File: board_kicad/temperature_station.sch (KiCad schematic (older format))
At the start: 3 parts, among them U1 WeMos_D1_mini, U2 DHT11

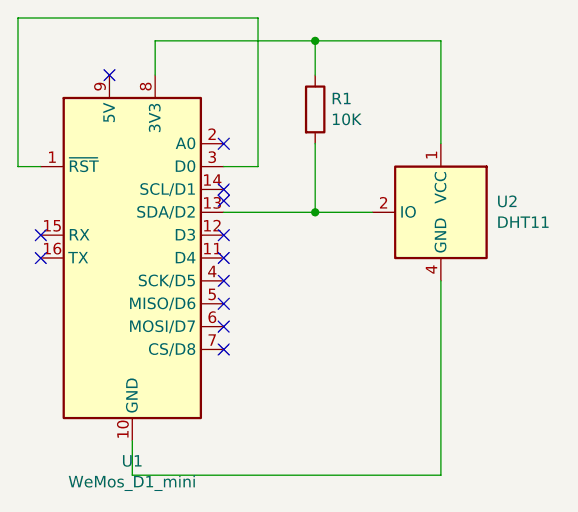
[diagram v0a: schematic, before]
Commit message: Changed DHT11 to DHT22
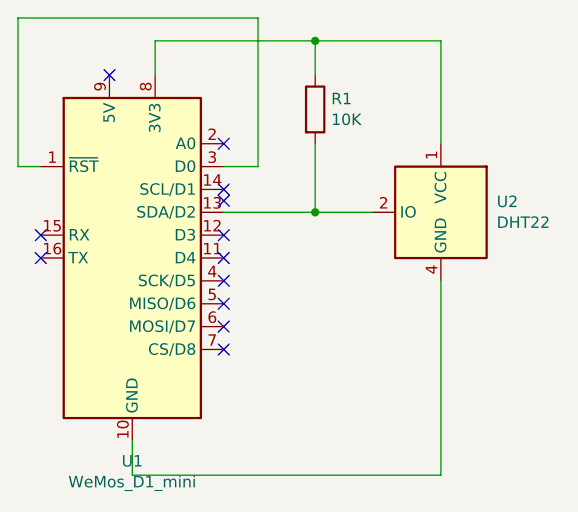
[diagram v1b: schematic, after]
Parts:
- U2: value DHT11 -> DHT22
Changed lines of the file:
@@
 P 5850 3700
 F 0 "U2" H 5606 3746 50  0000 R CNN
-F 1 "DHT11" H 5606 3655 50  0000 R CNN
+F 1 "DHT22" H 5606 3655 50  0000 R CNN
 F 2 "Sensor:Aosong_DHT11_5.5x12.0_P2.54mm" H 5850 3300 50  0001 C CNN
 F 3 "http://akizukidenshi.com/download/ds/aosong/DHT11.pdf" H 6000 3950 50  0001 C CNN
